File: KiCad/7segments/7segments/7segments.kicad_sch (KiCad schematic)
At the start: 19 parts, among them J1 Conn_01x04_Female, J2 12V DC, J3 R pinnen RGB strips, SW1 ENABLE, SW2 BOOT, T1 BC848, T2 BC848, T3 BC848, T4 BC848, T5 BC848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

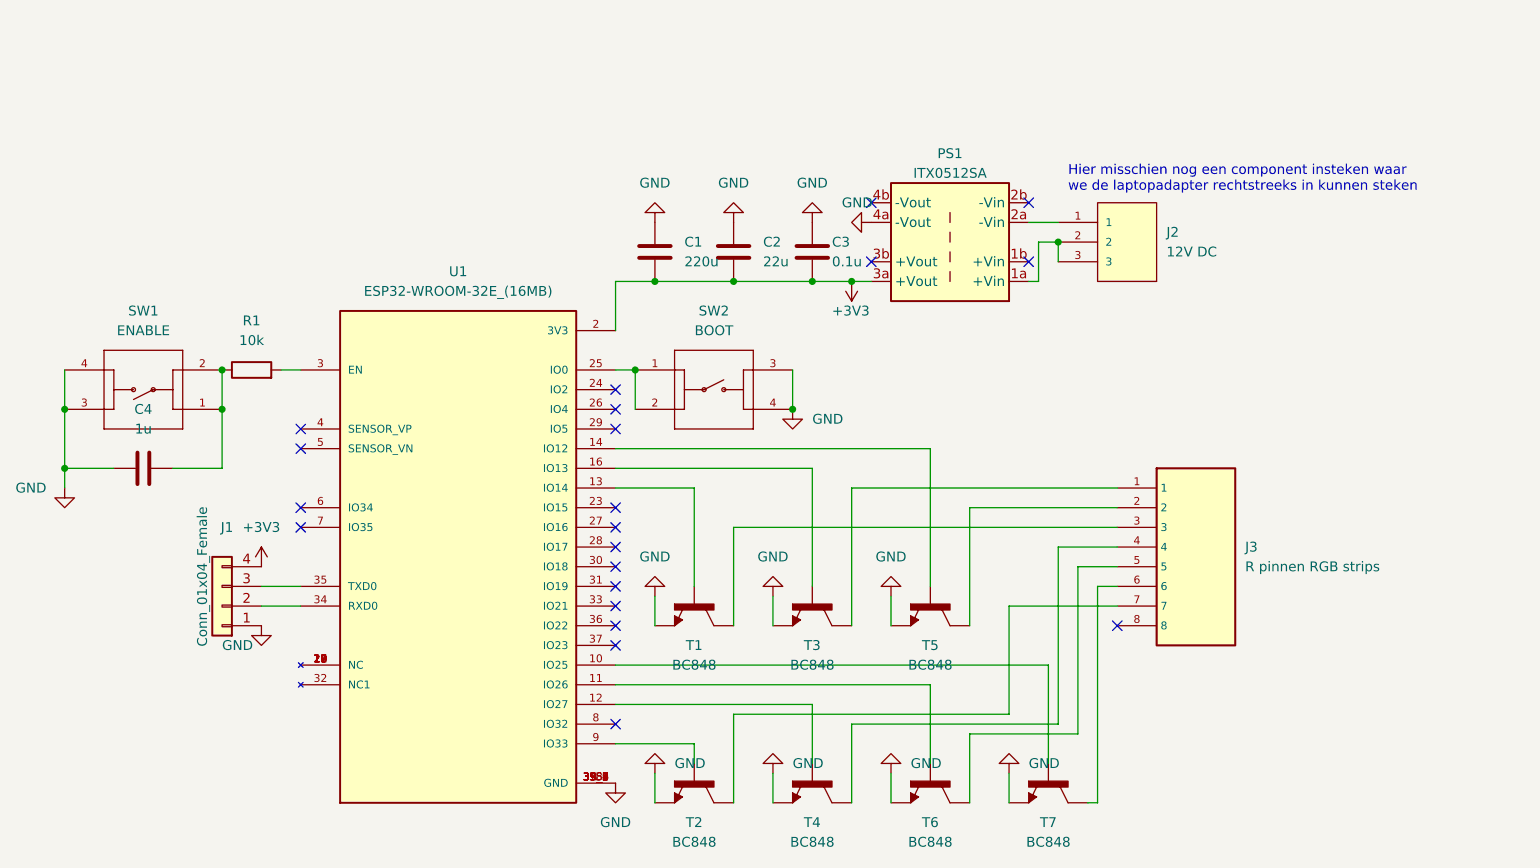
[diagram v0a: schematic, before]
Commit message: update buffer
enkel schema van de buffer is volledig in orde met LDO!!!
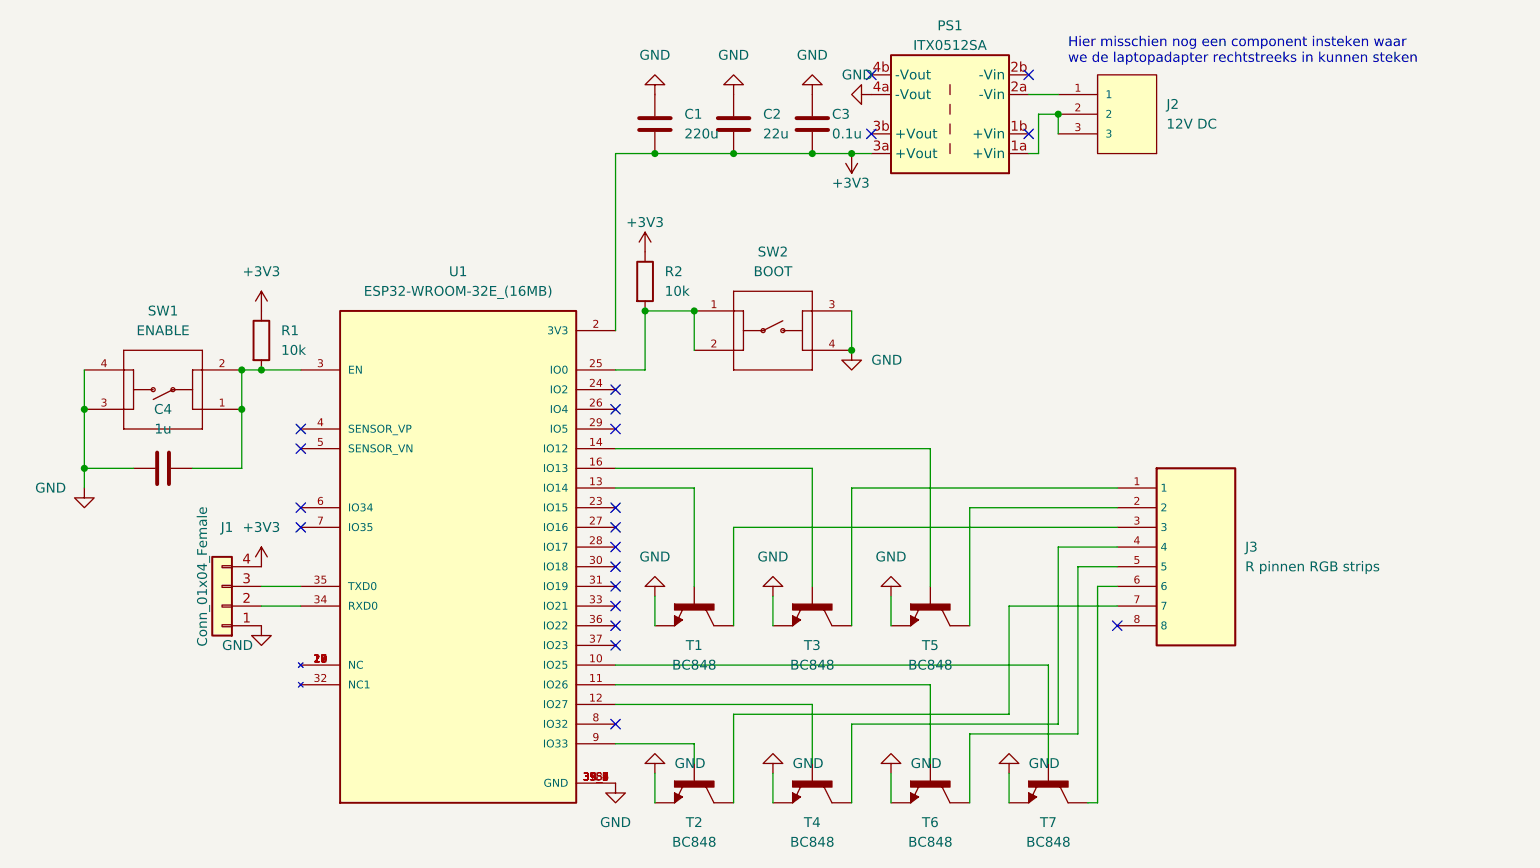
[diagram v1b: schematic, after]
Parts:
- added R2: 10k, Resistor_SMD:R_0805_2012Metric, symbol Device:R
- R1: footprint (none) -> Resistor_SMD:R_0805_2012Metric
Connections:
- net +3V3: now also R1.1, R2.1
- net at C4.2, SW1.1, SW1.2: now also R1.2, U1.3 (EN); no longer R1.1
- net at SW2.1, SW2.2, U1.25 (IO0): now also R2.2
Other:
- moved on the sheet: C1, C2, C3, J2, PS1
